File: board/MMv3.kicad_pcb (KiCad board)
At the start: 2 copper layers, 69 x 72 mm, 52 parts, among them J1 9V, J2 DRV8833_L, J3 left_mot, J4 right_mot, J5 DRV8833_R, Q1 DMG2301L, Q2 DMG2302U, Q3 DMG2302U, Q4 DMG2302U, SW1 PWR, SW2 but, U1 DS28E05R+T, U2 LD1117S50TR_SOT223, U3 RPi_Pico

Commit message: finished MMv3.2
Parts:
- removed the C2 at (120.0, 124.8)
- removed the R10 at (135.0, 74.2)
- removed R13, R15: 150, Resistor_SMD:R_0805_2012Metric
- removed R14: 10k, Resistor_SMD:R_0805_2012Metric
- removed the R5 at (129.5, 81.0)
- removed the R6 at (127.5, 81.0)
- added H3: MountingHole, MountingHole:MountingHole_3.2mm_M3_Pad_TopBottom, F.Cu at (120.0, 69.0)
- added H7: MountingHole, MountingHole:MountingHole_3.2mm_M3_Pad_TopBottom, F.Cu at (180.0, 69.0)
- D10, D11, D2, D3, D6, D7: footprint extraparts:LED_D3.00mm_RH_SMD -> extraparts:LED_D3.0mm_RH_THT_Clear
- D12, D4, D8: footprint extraparts:LED_D3.00mm_RH_SMD_ALT -> extraparts:LED_D3.0mm_RH_THT_IRBlack
- D13, D5, D9: footprint extraparts:LED_D3.00mm_RH_SMD -> extraparts:LED_D3.0mm_RH_THT_IRBlack
- moved R9 46.5 mm to (181.2, 81.0), turned to 90 degrees
- moved Q3 4.27 mm to (131.0, 70.0)
- moved R10 3.29 mm to (181.2, 119.0), turned to 270 degrees
- moved Q2 3.25 mm to (121.5, 81.0)
- moved Q4 3.25 mm to (178.5, 81.0), turned to 270 degrees
- moved R5 3.25 mm to (118.8, 119.0)
- moved R6 3.25 mm to (118.8, 81.0), turned to 90 degrees
- moved R7 3.25 mm to (131.0, 67.2)
- moved R8 3.25 mm to (169.0, 67.2), turned to 0 degrees
- moved D12 1.77 mm to (183.5, 76.8), turned to 270 degrees
- moved D13 1.77 mm to (183.5, 123.2), turned to 270 degrees
- moved D4 1.77 mm to (116.5, 123.2), turned to 90 degrees
- moved D5 1.77 mm to (116.5, 76.8), turned to 90 degrees
- moved D8 1.77 mm to (126.8, 65.0), turned to 0 degrees
- moved D9 1.77 mm to (173.2, 65.0), turned to 0 degrees
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- renumbered C3 to C2, H5 to H4, H3 to H5, H4 to H6, H6 to H8, R16 to R10, R7 to R5, R8 to R6, R11 to R7, R12 to R8
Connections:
- Q2 pad 1: Net-(Q2-Pad1) -> /lir_en
- Q3 pad 1: Net-(Q3-Pad1) -> /cir_en
- Q4 pad 1: Net-(Q4-Pad1) -> /rir_en
- R9 pad 1: Net-(Q3-Pad1) -> +5V
- R9 pad 2: /cir_en -> Net-(D10-Pad2)
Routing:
- net +5V: track 210.6 -> 219.7 mm
- net /cir_en: track 33.6 -> 40.5 mm
- net Net-(Q4-Pad1): track 6.49 -> 0.00 mm
- net Net-(D6-Pad1): track 48.0 -> 41.7 mm
- net +9V: track 66.3 -> 72.2 mm
- net /rir_en: track 23.7 -> 29.3 mm
- net Net-(Q2-Pad1): track 5.30 -> 0.00 mm
- net Net-(Q3-Pad1): track 5.30 -> 0.00 mm
- net Net-(D10-Pad1): track 55.4 -> 60.6 mm, vias 2 -> 0
- net /lir_en: track 39.8 -> 44.8 mm
- net /+3V3A: track 12.0 -> 15.6 mm, vias 0 -> 3
- net /but: track 29.1 -> 25.8 mm
- net /cir_b: track 64.9 -> 62.5 mm, vias 2 -> 0
- net /rir_b: track 33.8 -> 31.6 mm
- net /lir_a: track 23.9 -> 25.7 mm
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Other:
- net class BigPower added: clearance 0.2, trace_width 0.64, via_dia 1.2, via_drill 0.6
- board text added: "MMv3.2 Matt Tran"
- board text removed: "MMv3.1 Matt Tran"

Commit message: progress on lab 3
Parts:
- D10, D11, D12, D13, D2, D3, D4, D5, D6, D7, D8, D9: moved to F.Cu
- R2, R3, R4: value 1M -> 10K
- turned D10 to 90 degrees
- turned D11 to 90 degrees
- turned D12 to 90 degrees
- turned D13 to 90 degrees
- turned D2 to 270 degrees
- turned D3 to 270 degrees
- turned D4 to 270 degrees
- turned D5 to 270 degrees
- turned D6 to 180 degrees
- turned D7 to 180 degrees
- turned D8 to 180 degrees
- turned D9 to 180 degrees
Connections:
- D12 pad 1: /rir_a -> /r_adc
- D12 pad 2: /r_adc -> /rir_a
- D13 pad 1: /rir_b -> /r_adc
- D13 pad 2: /r_adc -> /rir_b
- D4 pad 1: /lir_a -> /l_adc
- D4 pad 2: /l_adc -> /lir_a
- D5 pad 1: /lir_b -> /l_adc
- D5 pad 2: /l_adc -> /lir_b
- D8 pad 1: /cir_a -> /c_adc
- D8 pad 2: /c_adc -> /cir_a
- D9 pad 1: /cir_b -> /c_adc
- D9 pad 2: /c_adc -> /cir_b
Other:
- board text added: "MMv3.3 Matt Tran"
- board text removed: "MMv3.2 Matt Tran"

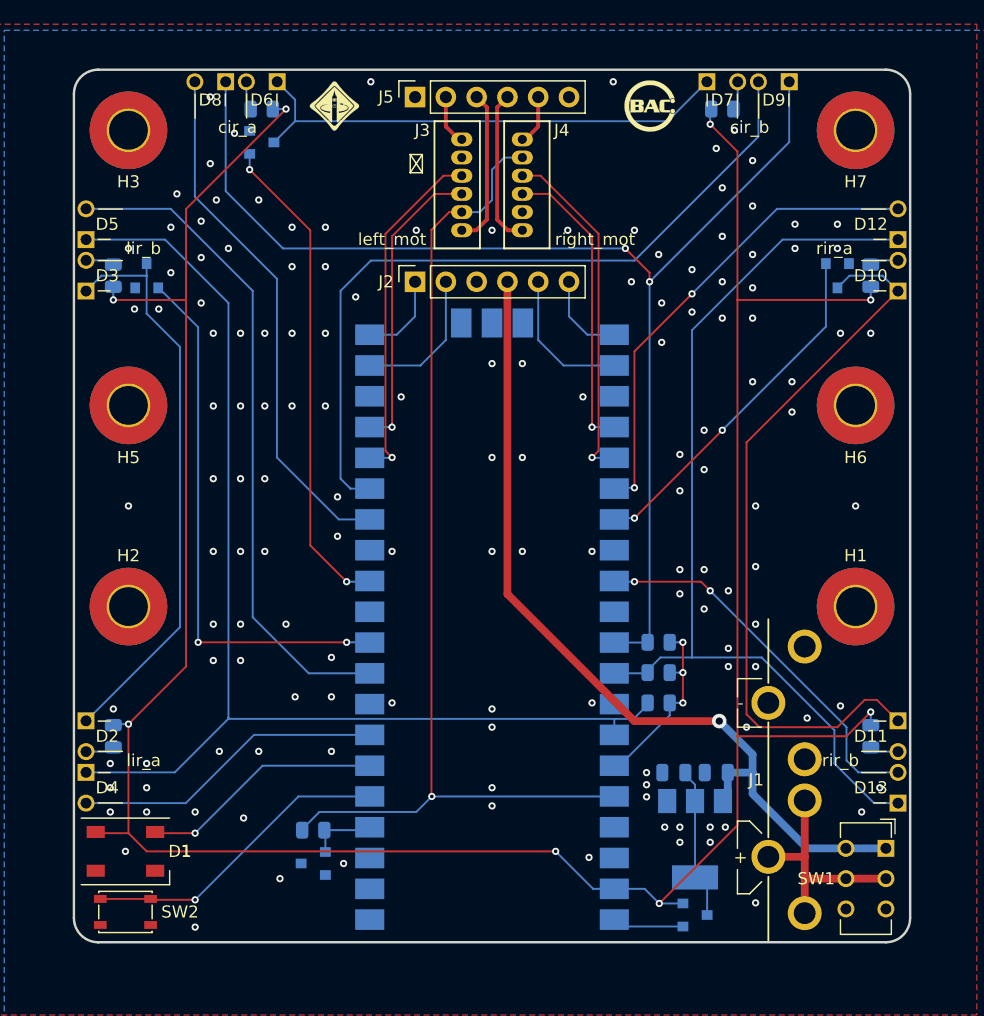
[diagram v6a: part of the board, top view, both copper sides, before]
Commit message: convert to kicad 6
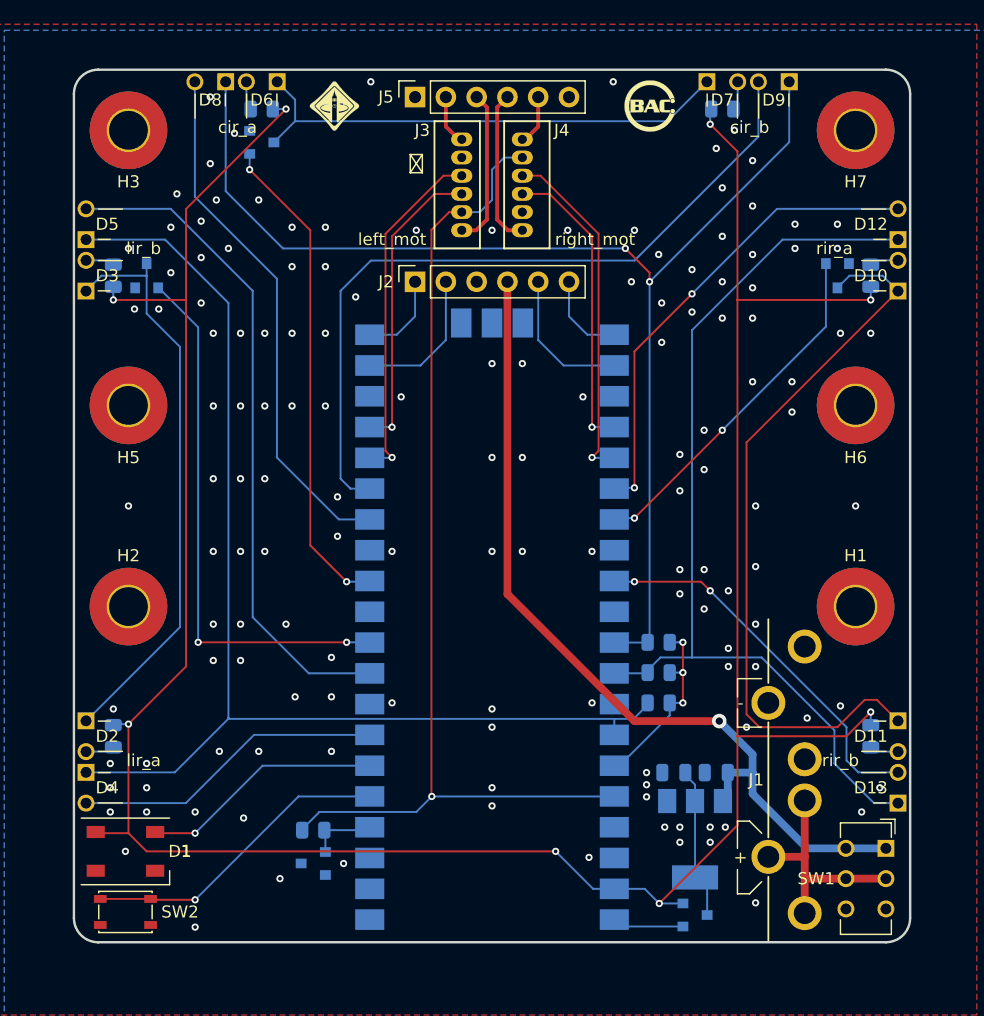
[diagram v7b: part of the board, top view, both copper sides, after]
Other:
- net class BigPower removed
- net class Default removed
- net class Power removed

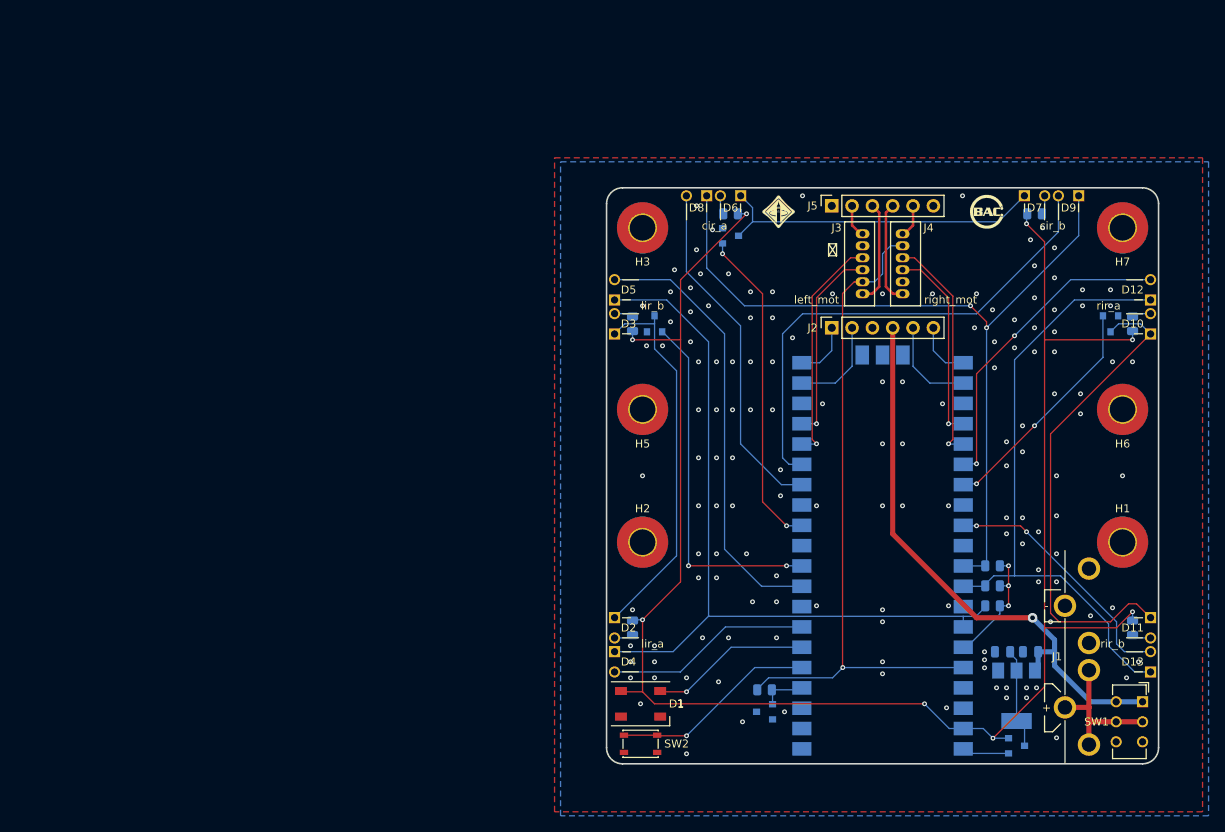
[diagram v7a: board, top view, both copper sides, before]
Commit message: adapt to BAC standard capability
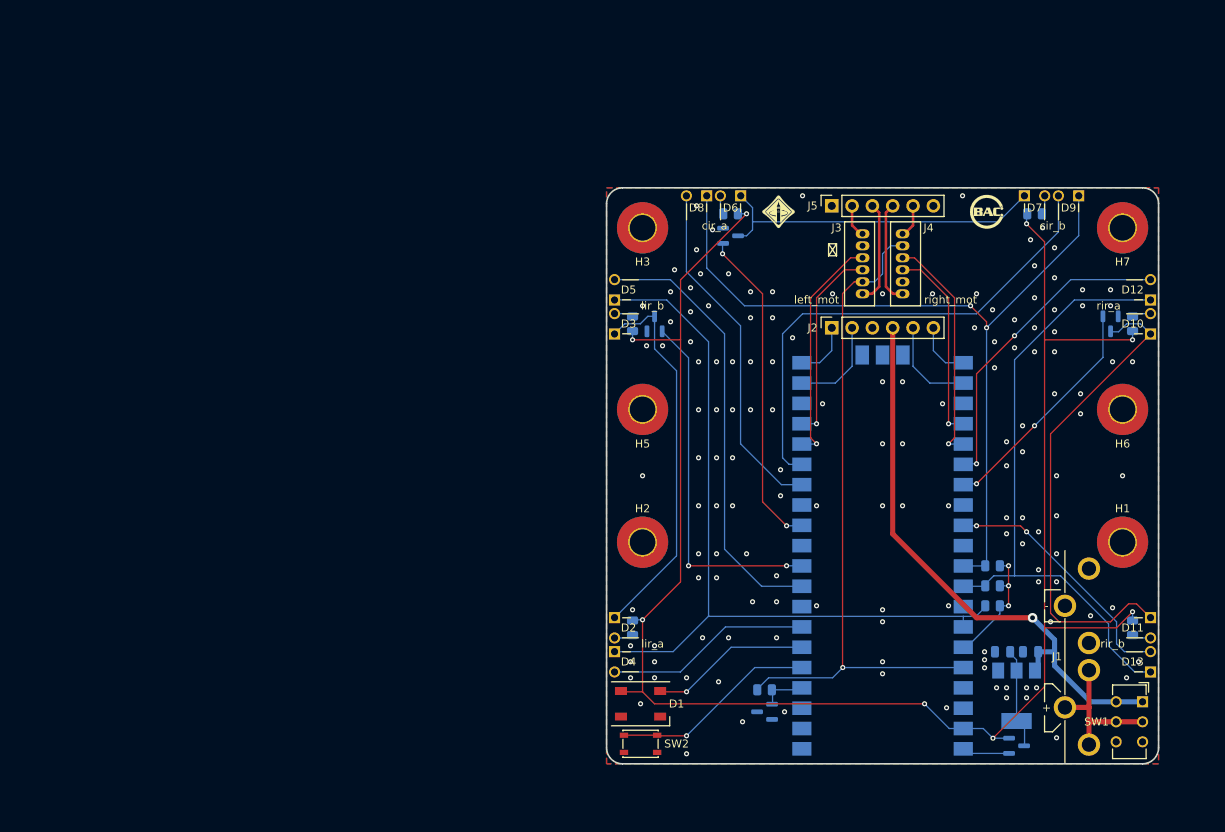
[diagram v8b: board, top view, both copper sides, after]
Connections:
- D1 pad 2: Net-(D1-Pad2) -> unconnected-(D1-Pad2)
- J5 pad 1: Net-(J5-Pad1) -> unconnected-(J5-Pad1)
- J5 pad 6: Net-(J5-Pad6) -> unconnected-(J5-Pad6)
- SW1 pad 3: Net-(SW1-Pad3) -> unconnected-(SW1-Pad3)
- SW1 pad 6: Net-(SW1-Pad6) -> unconnected-(SW1-Pad6)
- U1 pad 2: Net-(U1-Pad2) -> unconnected-(U1-Pad2)
- U3 pad 1: Net-(U3-Pad1) -> unconnected-(U3-Pad1)
- U3 pad 11: Net-(U3-Pad11) -> unconnected-(U3-Pad11)
- U3 pad 2: Net-(U3-Pad2) -> unconnected-(U3-Pad2)
- U3 pad 30: Net-(U3-Pad30) -> unconnected-(U3-Pad30)
- U3 pad 37: Net-(U3-Pad37) -> unconnected-(U3-Pad37)
- U3 pad D1: Net-(U3-PadD1) -> unconnected-(U3-PadD1)
- U3 pad D3: Net-(U3-PadD3) -> unconnected-(U3-PadD3)
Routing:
- net Net-(D6-Pad1): track 41.7 -> 42.2 mm
